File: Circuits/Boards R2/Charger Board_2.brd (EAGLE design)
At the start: 63.5 x 50.8 mm, 65 parts, among them CON1 ISP(2X3), CON10 HEADER_3X1, CON11 HEADER_3X1, CON12 HEADER_3X1, CON2 SCREWTERMINAL_1X2, CON3 HEADER_3X1, CON4 HEADER_3X1, CON5 HEADER_3X1, CON6 HEADER_3X1, CON7 HEADER_3X1, CON8 HEADER_3X1, CON9 HEADER_3X1, IC1 NCP1117DT33G, T1 NPN2N2222, T2 NPN2N2222, T3 SI4421DY, U1 ATMEGA324P, U2 ACS711

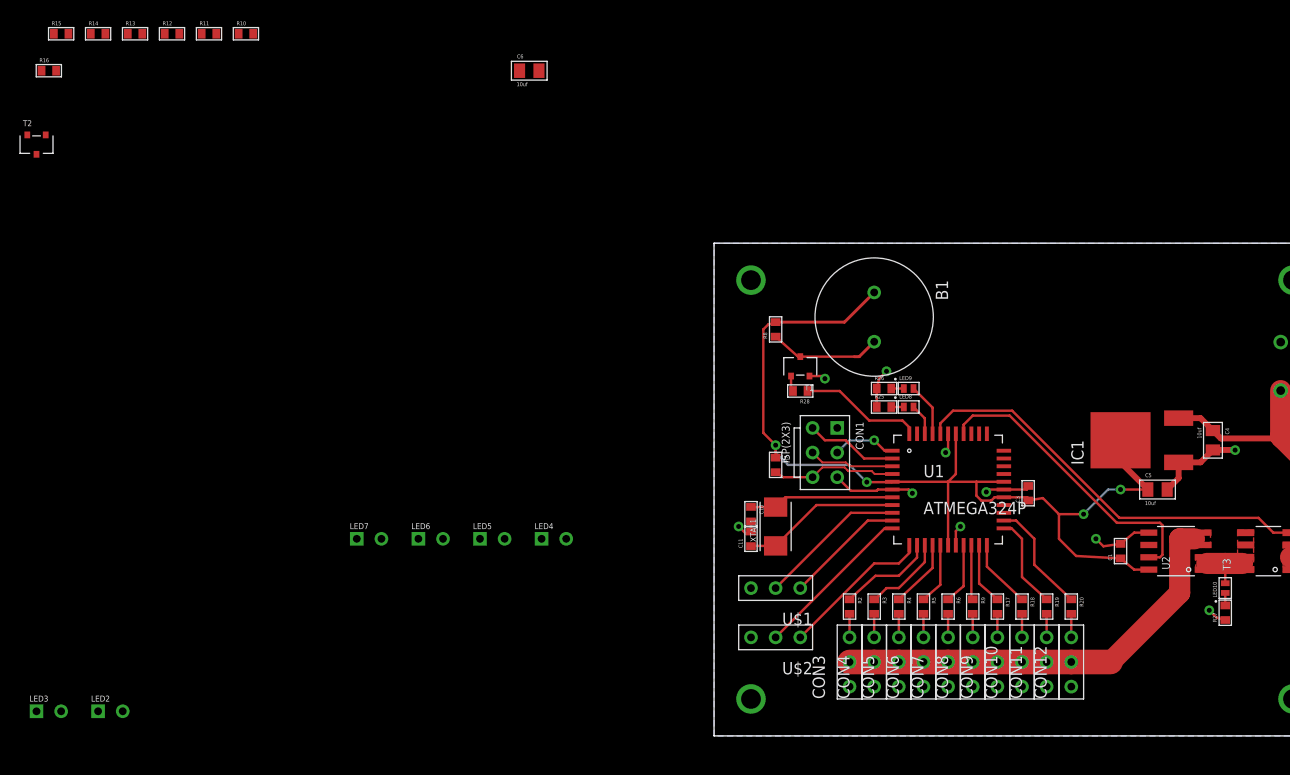
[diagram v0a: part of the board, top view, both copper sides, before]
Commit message: updated swarm board with R2 and started charger board changes
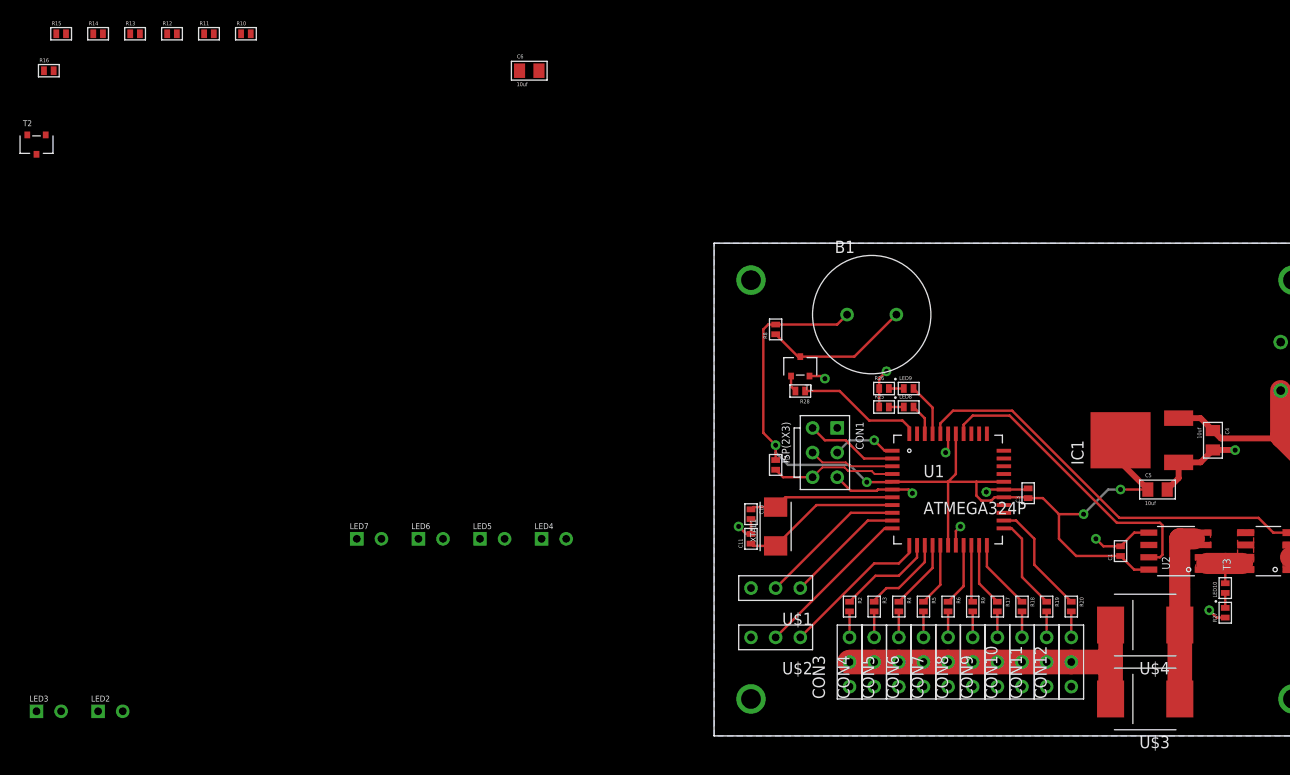
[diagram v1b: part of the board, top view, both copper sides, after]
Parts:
- added U$3, U$4: MBRS410LT3, Passive:SMD_DIODE
- B1: value PIEZOBUZZERPTH -> PIEZOBUZZER
- moved B1 0.36 mm to (16.3, 43.4), turned to 0 degrees
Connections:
- new net N$23: U$3.1, U$4.1, U2.3, U2.4
- net CHARGE+: now also U$3.2, U$4.2; no longer U2.3, U2.4
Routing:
- net N$23: track 0.00 -> 19.1 mm
- net CHARGE+: track 45.2 -> 34.5 mm
- net N$9: track 11.6 -> 15.2 mm
- net +3V3: track 104.8 -> 101.3 mm
- added copper zone on layer 1, net N$23
- removed copper zone on layer 1, net CHARGE+

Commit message: saving charger changes
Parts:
- removed LED8, LED9: (no value), Passive:LED0603
- removed R25, R26: 200, Passive:0603
- added C2, C7: .1uf, Passive:0603
- added LED1: SMD_RGB, Passive:PLCC4
- added R1: 310, Passive:0603
- added R21, R22: 200, Passive:0603
- B1: device Passive:PIEZOBUZZER -> Passive:PIEZOBUZZER_HORIZONTAL
- LED10: value (none) -> red
- R16: value 500 -> 1k
- R28: value (none) -> 1k
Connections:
- removed net N$20: LED8.1, R25.2
- removed net N$21: LED9.1, R26.2
- new net LED3: R1.1, U1.43
- new net N$37: LED1.1, R1.2
- new net N$38: LED1.3, R21.2
- new net N$39: LED1.4, R22.2
- new net SCL: U1.19
- new net SDA: U1.20
- net +3V3: now also B1.P$1, C2.1, C7.1, CON1.1; no longer B1.1
- net +5V: now also LED1.2
- net GND: now also C2.2, C7.2; no longer R25.1, R26.1
- net LED1: now also R21.1; no longer LED9.2
- net LED2: now also R22.1; no longer LED8.2
- net N$9: now also B1.P$2; no longer B1.2
- net SECTION10: now also U1.26; no longer U1.24
- net SECTION5: now also U1.21; no longer U1.19
- net SECTION6: now also U1.22; no longer U1.20
- net SECTION7: now also U1.23; no longer U1.21
- net SECTION8: now also U1.24; no longer U1.22
- net SECTION9: now also U1.25; no longer U1.23
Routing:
- net SECTION6: track 5.87 -> 0.18 mm
- net SECTION5: track 6.48 -> 2.09 mm
- net GND: track 44.0 -> 39.6 mm, vias 10 -> 9
- net SECTION7: track 6.59 -> 2.49 mm
- net N$9: track 15.2 -> 11.4 mm
- net +3V3: track 101.3 -> 104.7 mm
- net LED1: track 5.48 -> 2.70 mm
- net SECTION8: track 7.31 -> 4.95 mm
- net LED2: track 3.24 -> 1.59 mm
- net N$21: track 1.54 -> 0.00 mm
- net N$20: track 1.54 -> 0.00 mm
- net SECTION10: track 12.0 -> 10.5 mm
- net SECTION9: track 9.85 -> 8.89 mm

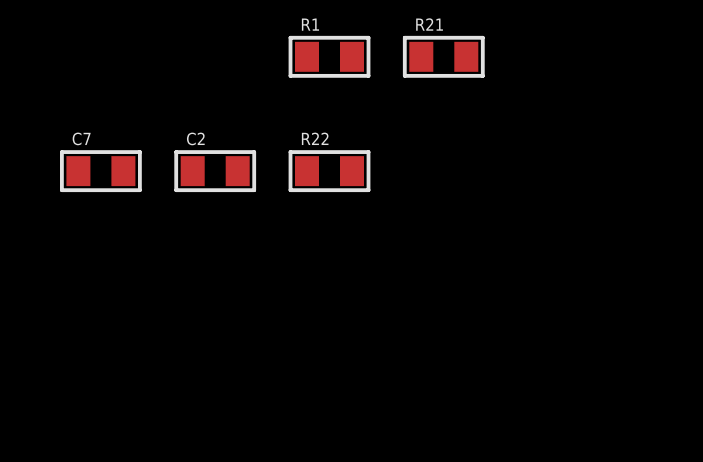
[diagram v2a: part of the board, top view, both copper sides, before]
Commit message: 
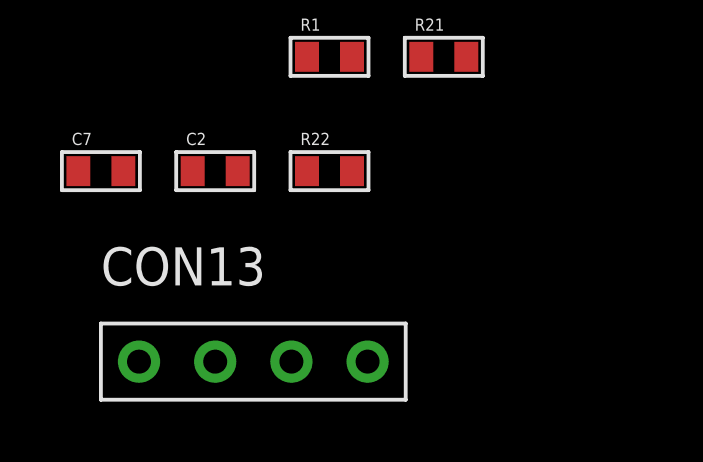
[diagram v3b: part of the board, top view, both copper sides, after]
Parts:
- added CON13: HEADER_4X1, Mechanical:4PINHEADER_.100"
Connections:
- net +3V3: now also CON13.1
- net GND: now also CON13.4
- net SCL: now also CON13.2
- net SDA: now also CON13.3
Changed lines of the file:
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@@
 <element name="C2" library="Passive" package="0603" value=".1uf" x="-73.66" y="-12.7"/>
 <element name="C7" library="Passive" package="0603" value=".1uf" x="-77.47" y="-12.7"/>
+<element name="CON13" library="Mechanical" package="4PINHEADER_.100&quot;" value="HEADER_4X1" x="-73.66" y="-19.05"/>
 </elements>
 <signals>
@@
 <contactref element="C7" pad="2"/>
 <contactref element="C2" pad="2"/>
-<wire x1="-72.91" y1="-12.7" x2="-76.72" y2="-12.7" width="0" layer="19" extent="1-1"/>
-<wire x1="-70.8" y1="61.96" x2="-72.91" y2="-12.7" width="0" layer="19" extent="1-1"/>
-<wire x1="-18.05" y1="68.58" x2="-70.8" y2="61.96" width="0" layer="19" extent="1-1"/>
-<wire x1="9.84" y1="37.1" x2="-18.05" y2="68.58" width="0" layer="19" extent="1-1"/>
+<contactref element="CON13" pad="4"/>
+<wire x1="53.705" y1="29.48" x2="58.42" y2="40.6" width="0" layer="19" extent="1-1"/>
+<wire x1="44.825" y1="20.955" x2="46.72" y2="25.4" width="0" layer="19" extent="1-1"/>
+<wire x1="32.25" y1="25.4" x2="39.37" y2="20.32" width="0" layer="19" extent="1-1"/>
+<wire x1="25.4" y1="21.59" x2="28.067" y2="25.146" width="0" layer="19" extent="1-1"/>
+<wire x1="24.13" y1="29.464" x2="28.321" y2="25.4" width="0" layer="19" extent="1-1"/>
+<wire x1="20.066" y1="25.4" x2="23.876" y2="29.21" width="0" layer="19" extent="1-1"/>
+<wire x1="3.81" y1="22.11" x2="12.7" y2="26.67" width="0" layer="19" extent="1-1"/>
+<wire x1="3.81" y1="15.24" x2="3.31" y2="20.82" width="0" layer="19" extent="1-1"/>
+<wire x1="3.81" y1="10.16" x2="3.81" y2="15.24" width="0" layer="19" extent="1-1"/>
+<wire x1="51.054" y1="12.954" x2="44.825" y2="20.955" width="0" layer="19" extent="1-1"/>
+<wire x1="11.43" y1="36.83" x2="12.7" y2="26.67" width="0" layer="19" extent="1-1"/>
+<wire x1="13.97" y1="5.08" x2="3.81" y2="10.16" width="0" layer="19" extent="1-1"/>
+<wire x1="16.51" y1="5.08" x2="13.97" y2="5.08" width="0" layer="19" extent="1-1"/>
+<wire x1="19.05" y1="5.08" x2="16.51" y2="5.08" width="0" layer="19" extent="1-1"/>
+<wire x1="21.59" y1="5.08" x2="19.05" y2="5.08" width="0" layer="19" extent="1-1"/>
+<wire x1="24.13" y1="5.08" x2="21.59" y2="5.08" width="0" layer="19" extent="1-1"/>
+<wire x1="26.67" y1="5.08" x2="24.13" y2="5.08" width="0" layer="19" extent="1-1"/>
+<wire x1="29.21" y1="5.08" x2="26.67" y2="5.08" width="0" layer="19" extent="1-1"/>
+<wire x1="31.75" y1="5.08" x2="29.21" y2="5.08" width="0" layer="19" extent="1-1"/>
+<wire x1="34.29" y1="5.08" x2="31.75" y2="5.08" width="0" layer="19" extent="1-1"/>
+<wire x1="36.83" y1="5.08" x2="34.29" y2="5.08" width="0" layer="19" extent="1-1"/>
+<wire x1="-18.05" y1="68.58" x2="9.84" y2="37.1" width="0" layer="19" extent="1-1"/>
+<wire x1="-70.8" y1="61.96" x2="-18.05" y2="68.58" width="0" layer="19" extent="1-1"/>
+<wire x1="-72.91" y1="-12.7" x2="-70.8" y2="61.96" width="0" layer="19" extent="1-1"/>
+<wire x1="-76.72" y1="-12.7" x2="-72.91" y2="-12.7" width="0" layer="19" extent="1-1"/>
+<wire x1="-68.58" y1="-19.05" x2="-72.91" y2="-12.7" width="0" layer="19" extent="1-1"/>
 </signal>
 <signal name="N$2">
@@
 <contactref element="C7" pad="1"/>
 <contactref element="C2" pad="1"/>
-<wire x1="-74.41" y1="-12.7" x2="-78.22" y2="-12.7" width="0" layer="19" extent="1-1"/>
+<contactref element="CON13" pad="1"/>
+<wire x1="-74.41" y1="-12.7" x2="-76.2" y2="-19.05" width="0" layer="19" extent="1-1"/>
+<wire x1="-78.22" y1="-12.7" x2="-74.41" y2="-12.7" width="0" layer="19" extent="1-1"/>
 <wire x1="-69.85" y1="2.54" x2="-74.41" y2="-12.7" width="0" layer="19" extent="1-1"/>
 <wire x1="-63.5" y1="2.54" x2="-69.85" y2="2.54" width="0" layer="19" extent="1-1"/>
@@
 <signal name="SCL">
 <contactref element="U1" pad="19"/>
+<contactref element="CON13" pad="2"/>
+<wire x1="25.73" y1="19.65" x2="-73.66" y2="-19.05" width="0" layer="19" extent="1-1"/>
 </signal>
 <signal name="SDA">
 <contactref element="U1" pad="20"/>
+<contactref element="CON13" pad="3"/>
+<wire x1="26.53" y1="19.65" x2="-71.12" y2="-19.05" width="0" layer="19" extent="1-1"/>
 </signal>
 </signals>

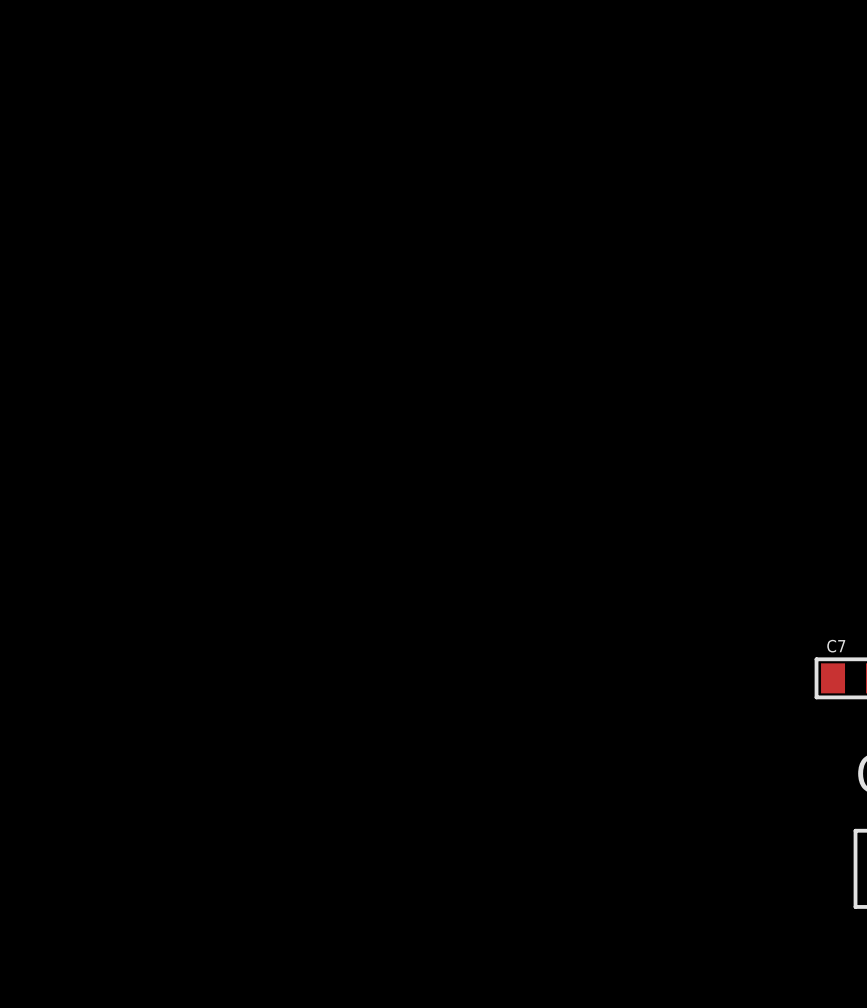
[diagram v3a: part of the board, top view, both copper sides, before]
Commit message: 
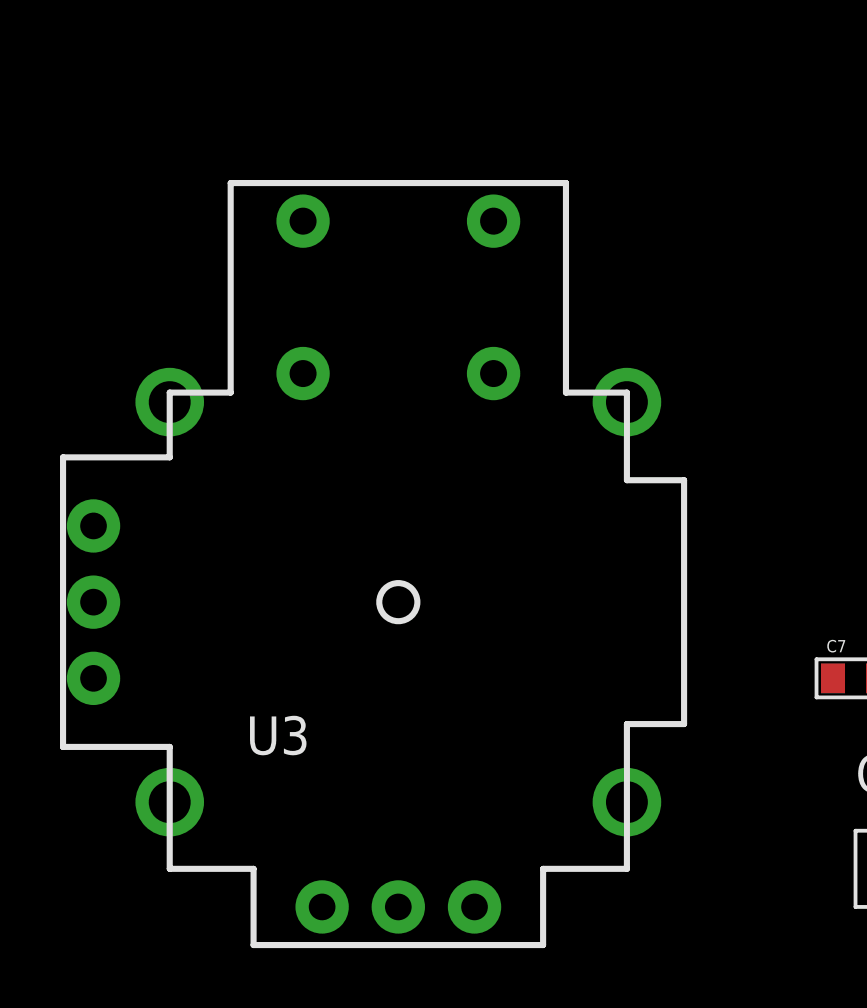
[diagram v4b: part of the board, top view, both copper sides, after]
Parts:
- added U3: JOYSTICKPTH, SparkFun:JOYSTICK
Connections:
- net +3V3: no longer CON13.1
- net +5V: now also CON13.1
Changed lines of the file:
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@@
 <layer number="51" name="tDocu" color="7" fill="1" visible="yes" active="yes"/>
 <layer number="52" name="bDocu" color="7" fill="1" visible="no" active="yes"/>
+<layer number="53" name="tGND_GNDA" color="7" fill="9" visible="no" active="no"/>
+<layer number="54" name="bGND_GNDA" color="1" fill="9" visible="no" active="no"/>
+<layer number="56" name="wert" color="7" fill="1" visible="no" active="yes"/>
 <layer number="91" name="Nets" color="2" fill="1" visible="no" active="no"/>
 <layer number="92" name="Busses" color="1" fill="1" visible="no" active="no"/>
@@
 <layer number="97" name="Info" color="7" fill="1" visible="no" active="no"/>
 <layer number="98" name="Guide" color="6" fill="1" visible="no" active="no"/>
+<layer number="100" name="Muster" color="7" fill="1" visible="no" active="no"/>
+<layer number="101" name="Patch_Top" color="12" fill="4" visible="no" active="yes"/>
+<layer number="102" name="Vscore" color="7" fill="1" visible="no" active="yes"/>
+<layer number="103" name="tMap" color="7" fill="1" visible="no" active="yes"/>
+<layer number="104" name="Name" color="16" fill="1" visible="no" active="yes"/>
+<layer number="105" name="tPlate" color="7" fill="1" visible="no" active="yes"/>
+<layer number="106" name="bPlate" color="7" fill="1" visible="no" active="yes"/>
+<layer number="107" name="Crop" color="7" fill="1" visible="no" active="yes"/>
+<layer number="116" name="Patch_BOT" color="9" fill="4" visible="no" active="yes"/>
+<layer number="121" name="_tsilk" color="7" fill="1" visible="no" active="yes"/>
+<layer number="122" name="_bsilk" color="7" fill="1" visible="no" active="yes"/>
+<layer number="125" name="_tNames" color="7" fill="1" visible="no" active="yes"/>
+<layer number="144" name="Drill_legend" color="7" fill="1" visible="no" active="yes"/>
+<layer number="151" name="HeatSink" color="7" fill="1" visible="no" active="yes"/>
 <layer number="200" name="200bmp" color="1" fill="10" visible="no" active="no"/>
+<layer number="201" name="201bmp" color="2" fill="10" visible="no" active="yes"/>
+<layer number="202" name="202bmp" color="3" fill="10" visible="no" active="yes"/>
+<layer number="203" name="203bmp" color="4" fill="10" visible="no" active="yes"/>
+<layer number="204" name="204bmp" color="5" fill="10" visible="no" active="yes"/>
+<layer number="205" name="205bmp" color="6" fill="10" visible="no" active="yes"/>
+<layer number="206" name="206bmp" color="7" fill="10" visible="no" active="yes"/>
+<layer number="207" name="207bmp" color="8" fill="10" visible="no" active="yes"/>
+<layer number="208" name="208bmp" color="9" fill="10" visible="no" active="yes"/>
+<layer number="209" name="209bmp" color="7" fill="1" visible="no" active="yes"/>
+<layer number="210" name="210bmp" color="7" fill="1" visible="no" active="yes"/>
+<layer number="211" name="211bmp" color="7" fill="1" visible="no" active="yes"/>
+<layer number="212" name="212bmp" color="7" fill="1" visible="no" active="yes"/>
+<layer number="213" name="213bmp" color="7" fill="1" visible="no" active="yes"/>
+<layer number="214" name="214bmp" color="7" fill="1" visible="no" active="yes"/>
+<layer number="215" name="215bmp" color="7" fill="1" visible="no" active="yes"/>
+<layer number="216" name="216bmp" color="7" fill="1" visible="no" active="yes"/>
+<layer number="217" name="217bmp" color="18" fill="1" visible="no" active="no"/>
+<layer number="218" name="218bmp" color="19" fill="1" visible="no" active="no"/>
+<layer number="219" name="219bmp" color="20" fill="1" visible="no" active="no"/>
+<layer number="220" name="220bmp" color="21" fill="1" visible="no" active="no"/>
+<layer number="221" name="221bmp" color="22" fill="1" visible="no" active="no"/>
+<layer number="222" name="222bmp" color="23" fill="1" visible="no" active="no"/>
+<layer number="223" name="223bmp" color="24" fill="1" visible="no" active="no"/>
+<layer number="224" name="224bmp" color="25" fill="1" visible="no" active="no"/>
+<layer number="250" name="Descript" color="3" fill="1" visible="no" active="no"/>
+<layer number="251" name="SMDround" color="12" fill="11" visible="no" active="no"/>
+<layer number="254" name="cooling" color="7" fill="1" visible="no" active="yes"/>
 </layers>
 <board>
@@
 <element name="C7" library="Passive" package="0603" value=".1uf" x="-77.47" y="-12.7"/>
 <element name="CON13" library="Mechanical" package="4PINHEADER_.100&quot;" value="HEADER_4X1" x="-73.66" y="-19.05"/>
+<element name="U3" library="SparkFun" package="JOYSTICK" value="JOYSTICKPTH" x="-92.71" y="-10.16"/>
 </elements>
 <signals>
@@
 <wire x1="52.2445" y1="30.6705" x2="58.6105" y2="30.6705" width="0.6096" layer="1"/>
 <contactref element="LED1" pad="2"/>
+<contactref element="CON13" pad="1"/>
+<wire x1="-70.08" y1="-5.88" x2="-76.2" y2="-19.05" width="0" layer="19" extent="1-1"/>
 <wire x1="47.9" y1="32.76" x2="-70.08" y2="-5.88" width="0" layer="19" extent="1-1"/>
+<wire x1="59.49" y1="18.415" x2="59.49" y2="18.469" width="0" layer="19" extent="1-1"/>
+<wire x1="59.49" y1="17.145" x2="59.436" y2="18.415" width="0" layer="19" extent="1-1"/>
 </signal>
 <signal name="CURRENTSENSE">
@@
 <contactref element="C7" pad="1"/>
 <contactref element="C2" pad="1"/>
-<contactref element="CON13" pad="1"/>
-<wire x1="-74.41" y1="-12.7" x2="-76.2" y2="-19.05" width="0" layer="19" extent="1-1"/>
-<wire x1="-78.22" y1="-12.7" x2="-74.41" y2="-12.7" width="0" layer="19" extent="1-1"/>
+<wire x1="-74.41" y1="-12.7" x2="-78.22" y2="-12.7" width="0" layer="19" extent="1-1"/>
 <wire x1="-69.85" y1="2.54" x2="-74.41" y2="-12.7" width="0" layer="19" extent="1-1"/>
 <wire x1="-63.5" y1="2.54" x2="-69.85" y2="2.54" width="0" layer="19" extent="1-1"/>
